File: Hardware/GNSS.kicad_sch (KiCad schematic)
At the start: 31 parts, among them J1 U.FL_SMD, U13 74HC4052D, U2 mosaic-X5, U6 Power_Divider, U8 NEO-D9S

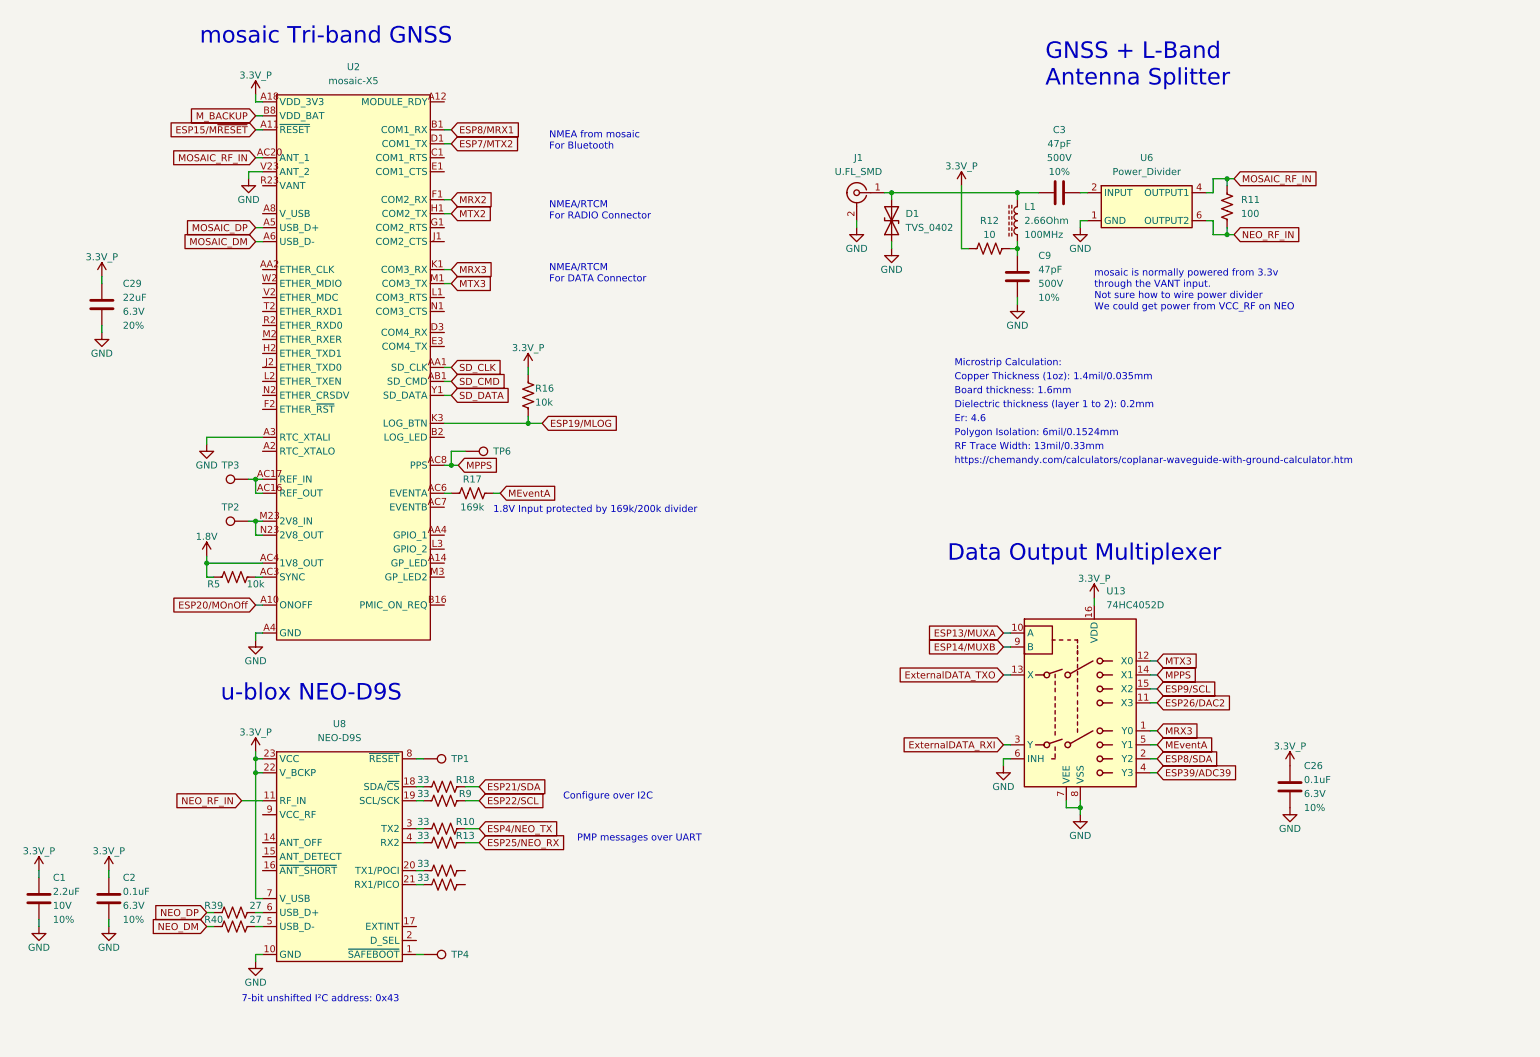
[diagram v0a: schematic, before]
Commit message: Schematic updates
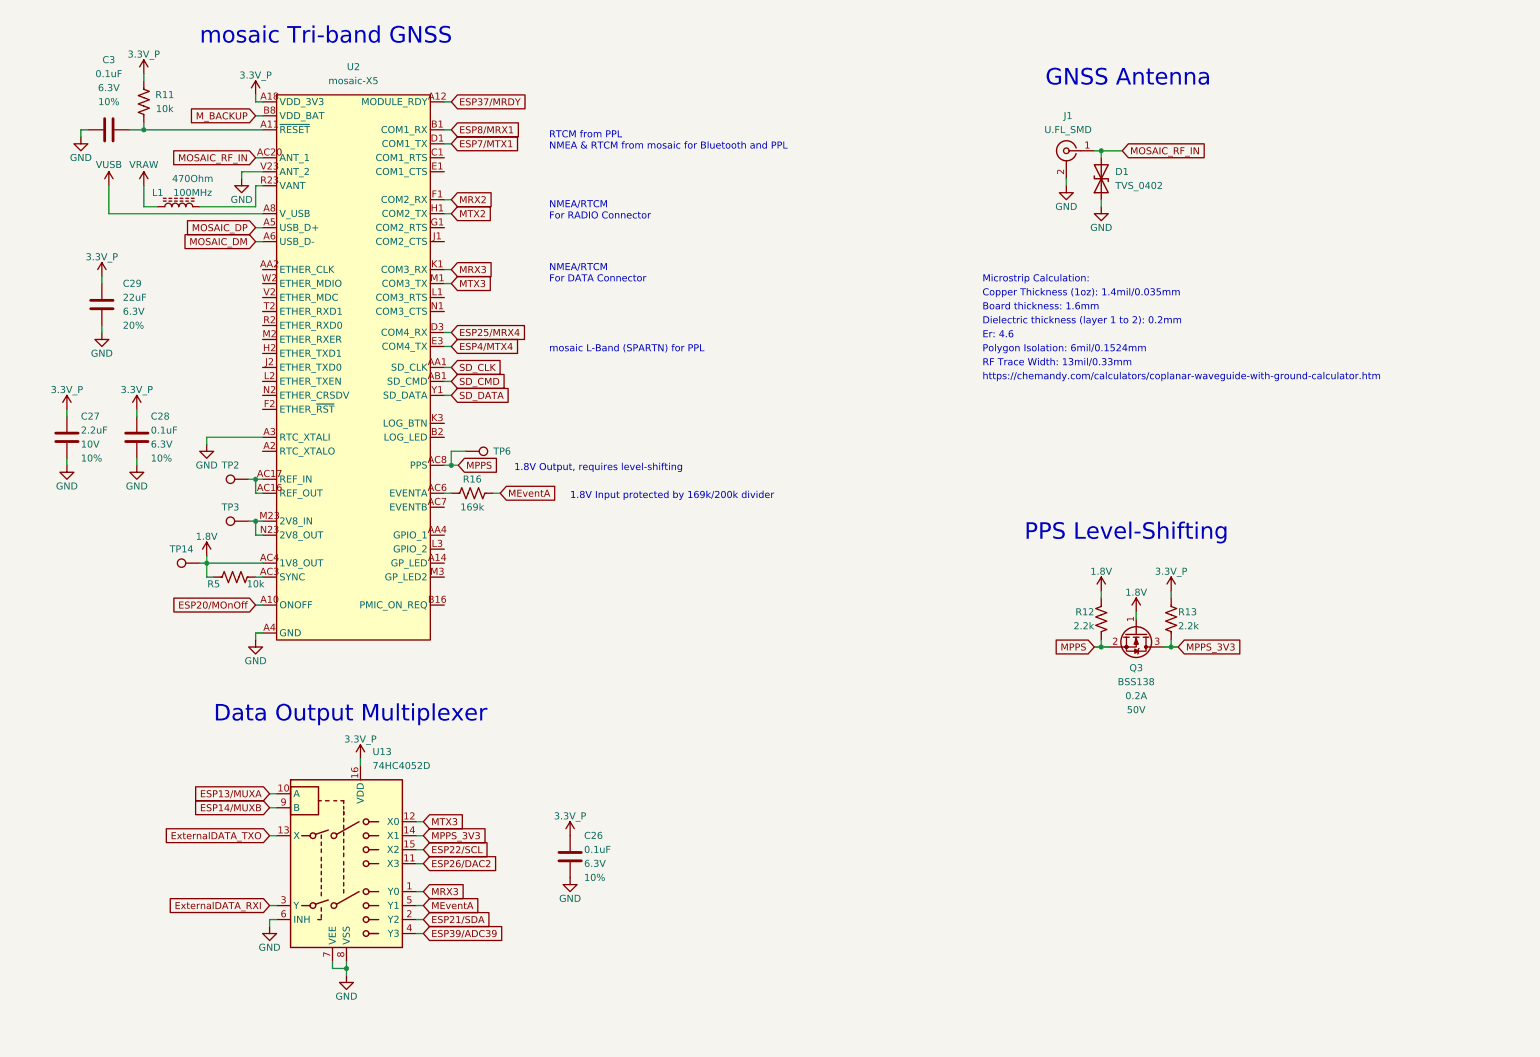
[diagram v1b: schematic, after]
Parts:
- removed C3, C9: 47pF, SparkFun-Capacitor:C_0402_1005Metric, symbol SparkFun-Capacitor:47pF_0402_500V_10%
- removed L1: 2.66Ohm, SparkFun-Capacitor:C_0603_1608Metric, symbol SparkFun-Coil:2.66Ohm_0402_110mA
- removed R10, R13, R14, R15, R18, R9: 33, SparkFun-Resistor:R_0402_1005Metric, symbol SparkFun-Resistor:33_0402
- removed R11: 100, SparkFun-Resistor:R_0402_1005Metric, symbol SparkFun-Resistor:100_0402
- removed R12: 10, SparkFun-Resistor:R_0402_1005Metric, symbol SparkFun-Resistor:10_0402
- removed R16: 10k, SparkFun-Resistor:R_0402_1005Metric, symbol SparkFun-Resistor:10k_0402
- removed R39, R40: 27, SparkFun-Resistor:R_0402_1005Metric, symbol SparkFun-Resistor:27_0402
- removed TP1, TP4: 1.0mm, SparkFun-Connector:TestPoint-1.0mm, symbol SparkFun-Connector:TestPoint_1.0mm
- removed U6: Power_Divider, SparkFun-RF:PD0922J5050S2HF_ANA, symbol SparkFun-RF:Power_Divider
- removed U8: NEO-D9S, SparkFun-GPS:NEO-M9N_M8T_M8U_D9S_F9P_F10N, symbol SparkFun-GPS:NEO-D9S
- added C3: 0.1uF, SparkFun-Capacitor:C_0402_1005Metric, symbol SparkFun-Capacitor:0.1uF_0402_6.3V_10%
- added L1: 470Ohm, SparkFun-Capacitor:C_0603_1608Metric, symbol SparkFun-Coil:470Ohm_0603_1.0A
- added Q3: BSS138, SparkFun-Semiconductor-Standard:SOT23-3, symbol SparkFun-DiscreteSemi:Q_NMOS_0.2A_50V
- added R11: 10k, SparkFun-Resistor:R_0402_1005Metric, symbol SparkFun-Resistor:10k_0402
- added R12, R13: 2.2k, SparkFun-Resistor:R_0402_1005Metric, symbol SparkFun-Resistor:2.2k_0402
- added TP14: 1.0mm, SparkFun-Connector:TestPoint-1.0mm, symbol SparkFun-Connector:TestPoint_1.0mm
- renumbered C1 to C27, C2 to C28, R17 to R16, TP3 to TP2, TP2 to TP3
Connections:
- net ESP8/SDA is gone; now on net ESP21/SDA: U13.2 (Y2)
- net ESP9/SCL is gone; now on net ESP22/SCL: U13.15 (X2)
- net 1.8V: now also Q3.1 (G), R12.1, TP14.1
- net 3.3V_P: now also R11.1, R13.1
- net GND: now also C3.2
- net MOSAIC_RF_IN: now also D1.2 (A2), J1.1 (In)
- net MPPS: now also Q3.2 (S), R12.2; no longer U13.14 (X1)
- net VANT: now also L1.2
- net ESP37/MRDY: now reaches U2.A12 (MODULE_RDY)
- net VUSB: now reaches U2.A8 (V_USB)
- net ESP25/MRX4: now reaches U2.D3 (COM4_RX)
- net ESP4/MTX4: now reaches U2.E3 (COM4_TX)
- net ESP15/M~{RESET}: no longer names the net of U2.A11 (~{RESET})
- net ESP15/M~{RESET}: now also C3.1, R11.2
- net ESP19/MLOG: no longer names the net of U2.K3 (LOG_BTN)
- net ESP7/MTX2 renamed ESP7/MTX1
- new net MPPS_3V3: Q3.3 (D), R13.2, U13.14 (X1)
- new net VRAW: L1.1
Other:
- note added: "1.8V Output, requires level-shifting"
- note added: "GNSS Antenna"
- note added: "PPS Level-Shifting"
- note added: "RTCM from PPL NMEA & RTCM from mosaic for Bluetooth and PPL"
- note added: "mosaic L-Band (SPARTN) for PPL"
- note removed: "7-bit unshifted I²C address: 0x43"
- note removed: "Configure over I2C"
- note removed: "GNSS + L-Band Antenna Splitter"
- note removed: "NMEA from mosaic For Bluetooth"
- note removed: "PMP messages over UART"
- note removed: "mosaic is normally powered from 3.3v through the VANT input. Not sure how to wire power divider We could get power from VCC_RF on NEO"
- note removed: "u-blox NEO-D9S"
- moved on the sheet: C26, C27, C28, D1, J1, U13

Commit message: Ready for airwire review
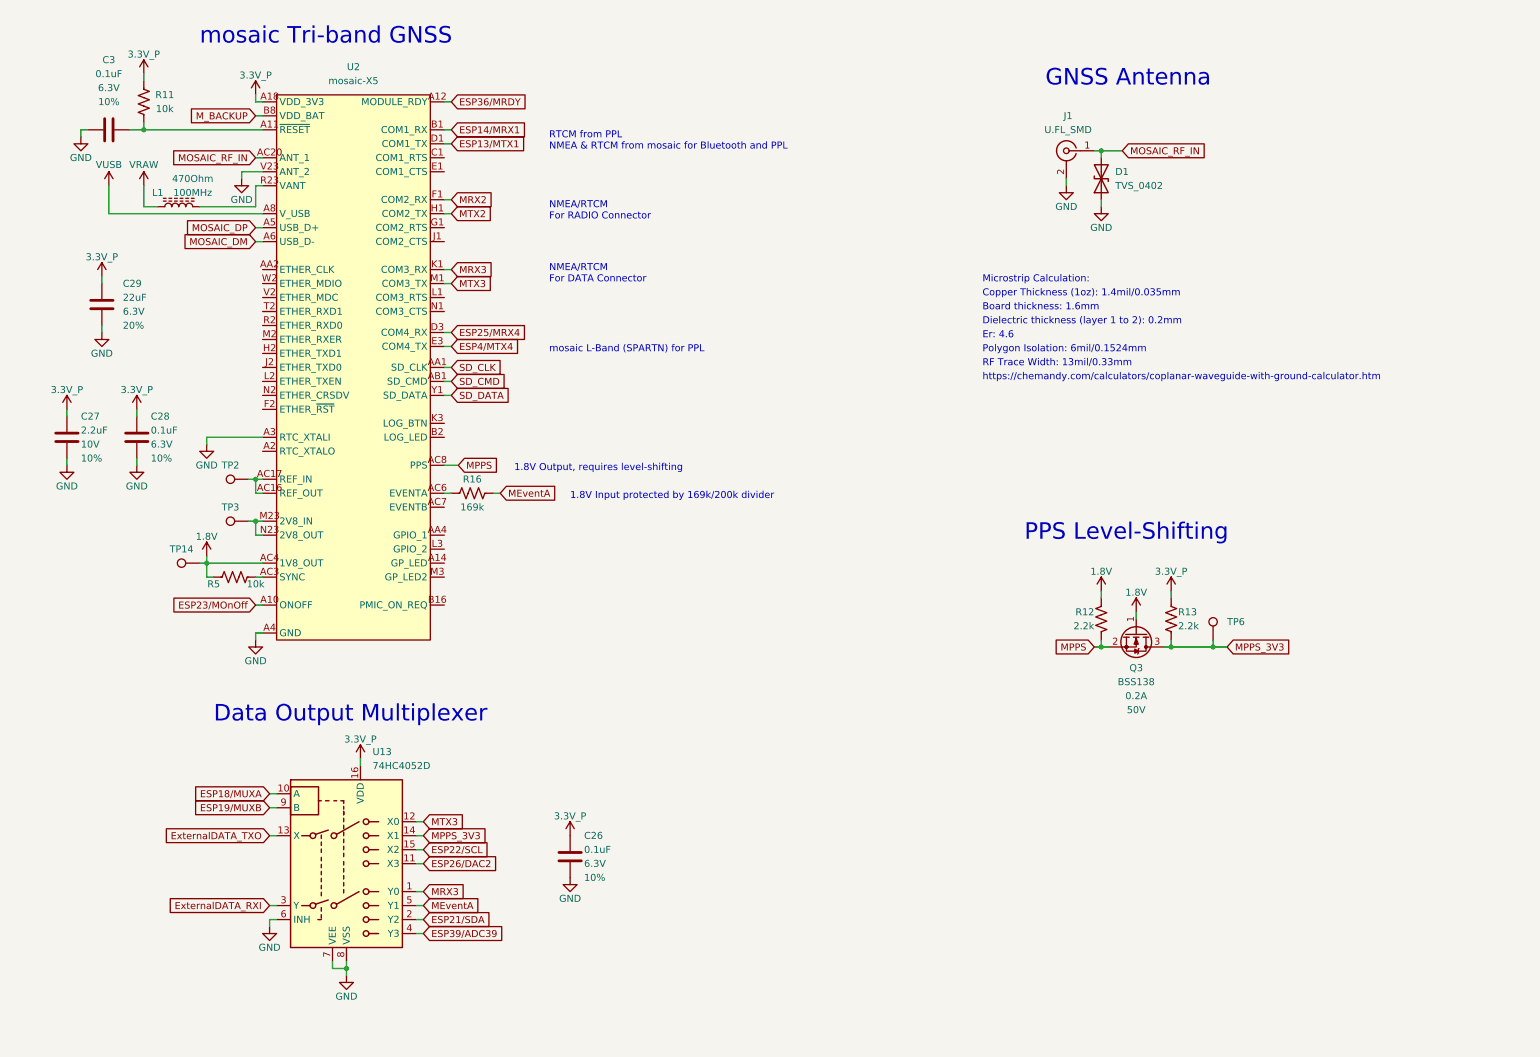
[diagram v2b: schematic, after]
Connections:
- net MPPS: no longer TP6.1
- net MPPS_3V3: now also TP6.1
- net ESP13/MUXA renamed ESP18/MUXA
- net ESP14/MUXB renamed ESP19/MUXB
- net ESP20/MOnOff renamed ESP23/MOnOff
- net ESP37/MRDY renamed ESP36/MRDY
- net ESP7/MTX1 renamed ESP13/MTX1
- net ESP8/MRX1 renamed ESP14/MRX1
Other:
- moved on the sheet: TP6
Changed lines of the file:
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@@
   (junction (at 57.15 97.79) (diameter 0) (color 0 0 0 0)
   )
-  (junction (at 92.71 95.25) (diameter 0) (color 0 0 0 0)
+  (junction (at 231.14 128.27) (diameter 0) (color 0 0 0 0)
   )
   (junction (at 210.82 128.27) (diameter 0) (color 0 0 0 0)
@@
     (stroke (width 0) (type default))
   )
+  (wire (pts (xy 231.14 128.27) (xy 233.68 128.27))
+    (stroke (width 0) (type default))
+  )
   (wire (pts (xy 73.66 185.42) (xy 73.66 186.69))
     (stroke (width 0) (type default))
@@
     (stroke (width 0) (type default))
   )
-  (wire (pts (xy 93.98 95.25) (xy 92.71 95.25))
+  (wire (pts (xy 91.44 95.25) (xy 93.98 95.25))
     (stroke (width 0) (type default))
   )
@@
     (stroke (width 0) (type default))
   )
-  (wire (pts (xy 92.71 95.25) (xy 91.44 95.25))
-    (stroke (width 0) (type default))
-  )
   (wire (pts (xy 48.26 115.57) (xy 48.26 113.03))
     (stroke (width 0) (type default))
@@
     (stroke (width 0) (type default))
   )
-  (wire (pts (xy 223.52 128.27) (xy 224.79 128.27))
+  (wire (pts (xy 223.52 128.27) (xy 231.14 128.27))
     (stroke (width 0) (type default))
   )
@@
     (stroke (width 0) (type default))
   )
-  (wire (pts (xy 92.71 92.71) (xy 92.71 95.25))
-    (stroke (width 0) (type default))
-  )
   (wire (pts (xy 30.48 49.53) (xy 58.42 49.53))
     (stroke (width 0) (type default))
@@
     (stroke (width 0) (type default))
   )
-  (wire (pts (xy 95.25 92.71) (xy 92.71 92.71))
-    (stroke (width 0) (type default))
-  )
   (wire (pts (xy 59.69 162.56) (xy 60.96 162.56))
     (stroke (width 0) (type default))
@@
   )
   (wire (pts (xy 58.42 100.33) (xy 57.15 100.33))
+    (stroke (width 0) (type default))
+  )
+  (wire (pts (xy 231.14 127) (xy 231.14 128.27))
     (stroke (width 0) (type default))
   )
@@
     )
   )
-  (global_label "ESP8{slash}MRX1" (shape input) (at 92.71 34.29 0) (fields_autoplaced)
+  (global_label "ESP14{slash}MRX1" (shape input) (at 92.71 34.29 0) (fields_autoplaced)
     (effects (font (size 1.27 1.27)) (justify left))
     (property "Intersheetrefs" "${INTERSHEET_REFS}" (at 107.0041 34.29 0)
@@
     )
   )
-  (global_label "ESP37{slash}MRDY" (shape input) (at 92.71 29.21 0) (fields_autoplaced)
+  (global_label "ESP36{slash}MRDY" (shape input) (at 92.71 29.21 0) (fields_autoplaced)
     (effects (font (size 1.27 1.27)) (justify left))
     (property "Intersheetrefs" "${INTERSHEET_REFS}" (at 108.1532 29.21 0)
@@
     )
   )
-  (global_label "MPPS_3V3" (shape input) (at 224.79 128.27 0) (fields_autoplaced)
-    (effects (font (size 1.27 1.27)) (justify left))
-    (property "Intersheetrefs" "${INTERSHEET_REFS}" (at 237.4513 128.27 0)
+  (global_label "MPPS_3V3" (shape input) (at 233.68 128.27 0) (fields_autoplaced)
+    (effects (font (size 1.27 1.27)) (justify left))
+    (property "Intersheetrefs" "${INTERSHEET_REFS}" (at 246.3413 128.27 0)
       (effects (font (size 1.27 1.27)) (justify left) hide)
     )
@@
     )
   )
-  (global_label "ESP14{slash}MUXB" (shape input) (at 59.69 157.48 180) (fields_autoplaced)
+  (global_label "ESP19{slash}MUXB" (shape input) (at 59.69 157.48 180) (fields_autoplaced)
     (effects (font (size 1.27 1.27)) (justify right))
     (property "Intersheetrefs" "${INTERSHEET_REFS}" (at 44.0654 157.48 0)
@@
     )
   )
-  (global_label "ESP20{slash}MOnOff" (shape input) (at 57.15 120.65 180) (fields_autoplaced)
+  (global_label "ESP23{slash}MOnOff" (shape input) (at 57.15 120.65 180) (fields_autoplaced)
     (effects (font (size 1.27 1.27)) (justify right))
     (property "Intersheetrefs" "${INTERSHEET_REFS}" (at 40.074 120.65 0)
@@
     )
   )
-  (global_label "ESP7{slash}MTX1" (shape input) (at 92.71 36.83 0) (fields_autoplaced)
+  (global_label "ESP13{slash}MTX1" (shape input) (at 92.71 36.83 0) (fields_autoplaced)
     (effects (font (size 1.27 1.27)) (justify left))
     (property "Intersheetrefs" "${INTERSHEET_REFS}" (at 106.7017 36.83 0)
@@
     )
   )
-  (global_label "ESP13{slash}MUXA" (shape input) (at 59.69 154.94 180) (fields_autoplaced)
+  (global_label "ESP18{slash}MUXA" (shape input) (at 59.69 154.94 180) (fields_autoplaced)
     (effects (font (size 1.27 1.27)) (justify right))
     (property "Intersheetrefs" "${INTERSHEET_REFS}" (at 44.2468 154.94 0)
@@
     )
   )
-  (symbol (lib_id "SparkFun-Connector:TestPoint_PTH") (at 95.25 92.71 270) (unit 1)
+  (symbol (lib_id "SparkFun-Connector:TestPoint_PTH") (at 231.14 127 0) (unit 1)
     (in_bom yes) (on_board yes) (dnp no) (fields_autoplaced)
-    (property "Reference" "TP6" (at 100.33 92.71 90)
-      (effects (font (size 1.27 1.27)) (justify left))
-    )
-    (property "Value" "PTH" (at 91.44 92.71 0)
-      (effects (font (size 1.27 1.27)) hide)
-    )
-    (property "Footprint" "SparkFun-Connector:1X01" (at 88.9 91.44 0)
-      (effects (font (size 1.27 1.27)) hide)
-    )
-    (property "Datasheet" "~" (at 87.63 92.71 0)
-      (effects (font (size 1.27 1.27)) hide)
-    )
+    (property "Reference" "TP6" (at 233.68 123.698 0)
+      (effects (font (size 1.27 1.27)) (justify left))
+    )
+    (property "Value" "PTH" (at 231.14 130.81 0)
+      (effects (font (size 1.27 1.27)) hide)
+    )
+    (property "Footprint" "SparkFun-Connector:1X01" (at 229.87 133.35 0)
+      (effects (font (size 1.27 1.27)) hide)
+    )
+    (property "Datasheet" "~" (at 231.14 134.62 0)
+      (effects (font (size 1.27 1.27)) hide)
+    )
